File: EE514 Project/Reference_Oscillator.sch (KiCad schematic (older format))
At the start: 4 parts

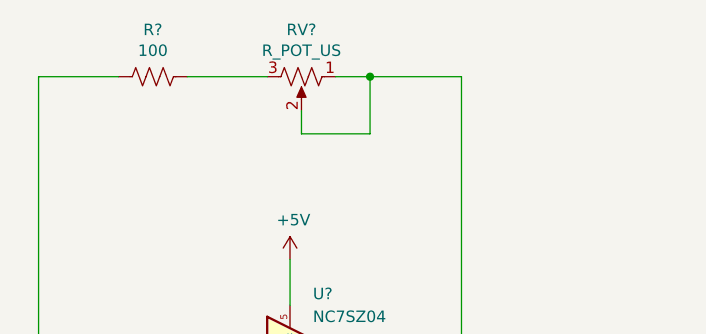
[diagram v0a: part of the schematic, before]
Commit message: Updated pot value
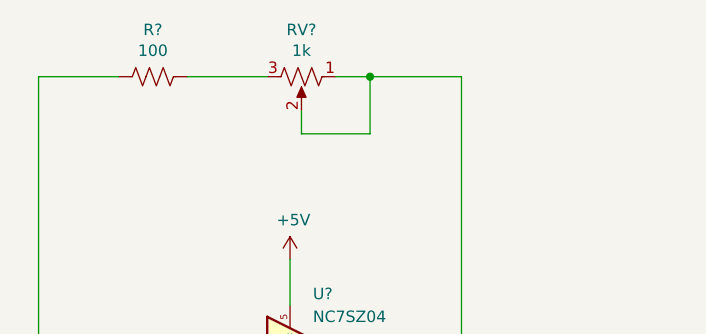
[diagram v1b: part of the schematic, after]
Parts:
- RV?: value R_POT_US -> 1k
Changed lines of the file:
@@
 P 5550 2650
 F 0 "RV?" V 5345 2650 50  0000 C CNN
-F 1 "R_POT_US" V 5436 2650 50  0000 C CNN
+F 1 "1k" V 5436 2650 50  0000 C CNN
 F 2 "irex_Potentiometer_THT:Potentiometer_Bourns_PV36W_Vertical" H 5550 2650 50  0001 C CNN
 F 3 "~" H 5550 2650 50  0001 C CNN

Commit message: Finished layout and generated gerbers
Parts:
- added C202: 0.1nF, EE514 Board:C_0603_1608Metric_Pad0.98x0.95mm_HandSolder, symbol Device:C
- added TP201: TestPoint, TestPoint:TestPoint_THTPad_D1.5mm_Drill0.7mm, symbol Connector:TestPoint
- C201: renamed from C?; footprint (none) -> EE514 Board:C_0603_1608Metric_Pad0.98x0.95mm_HandSolder
- R201: renamed from R?; footprint (none) -> EE514 Board:R_0603_1608Metric_Pad0.98x0.95mm_HandSolder; Digi-Key PN CR0603-FX-1000ELFCT-ND -> 311-100HRCT-ND
- gave numbers to parts that had none: 2
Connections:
- net +5V: now also C202.1
- net 10MHz_REF_OUT: now also TP201.1
- net GND: now also C202.2
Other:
- moved on the sheet: R201, RV201
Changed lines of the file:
@@
 $Descr A4 11693 8268
 encoding utf-8
-Sheet 2 2
+Sheet 2 4
 Title ""
 Date ""
@@
 $EndDescr
 $Comp
-L EE514_Board:NC7SZ04 U?
+L EE514_Board:NC7SZ04 U201
 U 1 1 61A0F24F
 P 5500 3850
-F 0 "U?" H 5600 4100 50  0000 L CNN
+F 0 "U201" H 5600 4100 50  0000 L CNN
 F 1 "NC7SZ04" H 5600 4000 50  0000 L CNN
 F 2 "Package_TO_SOT_SMD:SOT-23-5" H 5500 3600 50  0001 C CNN
@@
 $EndComp
 $Comp
-L power:GND #PWR?
+L power:GND #PWR0203
 U 1 1 61A101BF
 P 5500 4200
-F 0 "#PWR?" H 5500 3950 50  0001 C CNN
+F 0 "#PWR0203" H 5500 3950 50  0001 C CNN
 F 1 "GND" H 5505 4027 50  0000 C CNN
 F 2 "" H 5500 4200 50  0001 C CNN
@@
 	5500 4200 5500 4050
 Wire Wire Line
-	5500 3650 5500 3450
+	5500 3650 5500 2700
 $Comp
-L power:+5V #PWR?
+L power:+5V #PWR0202
 U 1 1 61A107C8
-P 5500 3450
-F 0 "#PWR?" H 5500 3300 50  0001 C CNN
-F 1 "+5V" H 5515 3623 50  0000 C CNN
-F 2 "" H 5500 3450 50  0001 C CNN
-F 3 "" H 5500 3450 50  0001 C CNN
-	1    5500 3450
+P 5500 2600
+F 0 "#PWR0202" H 5500 2450 50  0001 C CNN
+F 1 "+5V" H 5515 2773 50  0000 C CNN
+F 2 "" H 5500 2600 50  0001 C CNN
+F 3 "" H 5500 2600 50  0001 C CNN
+	1    5500 2600
 	1    0    0    -1
 $EndComp
 Wire Wire Line
-	5800 3850 6250 3850
+	5800 3850 6750 3850
 Wire Wire Line
-	6250 3850 6250 2650
+	6750 3850 6750 2000
 $Comp
-L Device:R_US R?
+L Device:R_US R201
 U 1 1 61A11308
-P 4900 2650
-F 0 "R?" V 4695 2650 50  0000 C CNN
-F 1 "100" V 4786 2650 50  0000 C CNN
-F 2 "" V 4940 2640 50  0001 C CNN
-F 3 "~" H 4900 2650 50  0001 C CNN
-F 4 "CR0603-FX-1000ELFCT-ND" H 4900 2650 50  0001 C CNN "Digi-Key PN"
-	1    4900 2650
+P 5200 2000
+F 0 "R201" V 4995 2000 50  0000 C CNN
+F 1 "100" V 5086 2000 50  0000 C CNN
+F 2 "EE514 Board:R_0603_1608Metric_Pad0.98x0.95mm_HandSolder" V 5240 1990 50  0001 C CNN
+F 3 "~" H 5200 2000 50  0001 C CNN
+F 4 "311-100HRCT-ND" H 5200 2000 50  0001 C CNN "Digi-Key PN"
+	1    5200 2000
 	0    1    1    0
 $EndComp
 Wire Wire Line
-	4750 2650 4400 2650
+	5050 2000 4400 2000
 Wire Wire Line
-	4400 2650 4400 3850
+	4400 2000 4400 3850
 Wire Wire Line
 	4400 3850 5300 3850
 $Comp
-L Device:C C?
+L Device:C C201
 U 1 1 61A16206
 P 4400 4250
-F 0 "C?" H 4515 4296 50  0000 L CNN
+F 0 "C201" H 4515 4296 50  0000 L CNN
 F 1 "0.1nF" H 4515 4205 50  0000 L CNN
-F 2 "" H 4438 4100 50  0001 C CNN
+F 2 "EE514 Board:C_0603_1608Metric_Pad0.98x0.95mm_HandSolder" H 4438 4100 50  0001 C CNN
 F 3 "~" H 4400 4250 50  0001 C CNN
 F 4 "399-C0603C101G1HAC7867CT-ND" H 4400 4250 50  0001 C CNN "Digi-Key PN"
@@
 $EndComp
 $Comp
-L power:GND #PWR?
+L power:GND #PWR0201
 U 1 1 61A16D78
 P 4400 4550
-F 0 "#PWR?" H 4400 4300 50  0001 C CNN
+F 0 "#PWR0201" H 4400 4300 50  0001 C CNN
 F 1 "GND" H 4405 4377 50  0000 C CNN
 F 2 "" H 4400 4550 50  0001 C CNN
@@
 Connection ~ 4400 3850
 Wire Wire Line
-	5050 2650 5400 2650
+	5350 2000 5800 2000
 $Comp
-L Device:R_POT_US RV?
+L Device:R_POT_US RV201
 U 1 1 61A129EF
-P 5550 2650
-F 0 "RV?" V 5345 2650 50  0000 C CNN
-F 1 "1k" V 5436 2650 50  0000 C CNN
-F 2 "irex_Potentiometer_THT:Potentiometer_Bourns_PV36W_Vertical" H 5550 2650 50  0001 C CNN
-F 3 "~" H 5550 2650 50  0001 C CNN
-F 4 "490-2874-ND" V 5437 2650 50  0001 C CNN "Digi-Key PN"
-	1    5550 2650
+P 5950 2000
+F 0 "RV201" V 5745 2000 50  0000 C CNN
+F 1 "1k" V 5836 2000 50  0000 C CNN
+F 2 "irex_Potentiometer_THT:Potentiometer_Bourns_PV36W_Vertical" H 5950 2000 50  0001 C CNN
+F 3 "~" H 5950 2000 50  0001 C CNN
+F 4 "490-2874-ND" V 5837 2000 50  0001 C CNN "Digi-Key PN"
+	1    5950 2000
 	0    1    1    0
 $EndComp
 Wire Wire Line
-	5550 2800 5550 2900
+	5950 2150 5950 2250
 Wire Wire Line
-	5550 2900 5850 2900
+	5950 2250 6250 2250
 Wire Wire Line
-	5850 2900 5850 2650
+	6250 2250 6250 2000
 Wire Wire Line
-	6250 2650 5850 2650
+	6750 2000 6250 2000
 Wire Wire Line
-	5850 2650 5700 2650
-Connection ~ 5850 2650
+	6250 2000 6100 2000
+Connection ~ 6250 2000
 Wire Wire Line
-	6250 3850 6700 3850
-Connection ~ 6250 3850
-Text HLabel 6700 3850 2    50   Output ~ 0
+	6750 3850 7100 3850
+Connection ~ 6750 3850
+Text HLabel 7400 3850 2    50   Output ~ 0
 10MHz_REF_OUT
+$Comp
+L Device:C C202
+U 1 1 61A8CF2C
+P 5750 2950
+F 0 "C202" H 5865 2996 50  0000 L CNN
+F 1 "0.1nF" H 5865 2905 50  0000 L CNN
+F 2 "EE514 Board:C_0603_1608Metric_Pad0.98x0.95mm_HandSolder" H 5788 2800 50  0001 C CNN
+F 3 "~" H 5750 2950 50  0001 C CNN
+F 4 "399-C0603C101G1HAC7867CT-ND" H 5750 2950 50  0001 C CNN "Digi-Key PN"
+	1    5750 2950
+	1    0    0    -1
+$EndComp
+Wire Wire Line
+	5750 2800 5750 2700
+Wire Wire Line
+	5750 2700 5500 2700
+Connection ~ 5500 2700
+Wire Wire Line
+	5500 2700 5500 2600
+$Comp
+L power:GND #PWR0204
+U 1 1 61A8E398
+P 5750 3200
+F 0 "#PWR0204" H 5750 2950 50  0001 C CNN
+F 1 "GND" H 5755 3027 50  0000 C CNN
+F 2 "" H 5750 3200 50  0001 C CNN
+F 3 "" H 5750 3200 50  0001 C CNN
+	1    5750 3200
+	1    0    0    -1
+$EndComp
+Wire Wire Line
+	5750 3200 5750 3100
+$Comp
+L Connector:TestPoint TP201
+U 1 1 61BAAEB4
+P 7100 3650
+F 0 "TP201" H 7158 3768 50  0000 L CNN
+F 1 "TestPoint" H 7158 3677 50  0000 L CNN
+F 2 "TestPoint:TestPoint_THTPad_D1.5mm_Drill0.7mm" H 7300 3650 50  0001 C CNN
+F 3 "~" H 7300 3650 50  0001 C CNN
+	1    7100 3650
+	1    0    0    -1
+$EndComp
+Wire Wire Line
+	7100 3650 7100 3850
+Connection ~ 7100 3850
+Wire Wire Line
+	7100 3850 7400 3850
 $EndSCHEMATC
